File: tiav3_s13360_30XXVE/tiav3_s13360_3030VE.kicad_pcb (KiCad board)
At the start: 4 copper layers, 25.3 x 25.3 mm, 24 parts, among them J1 SSQ-103-01-G-D, J2 Conn_Coaxial, U1 OPA847IDBVT

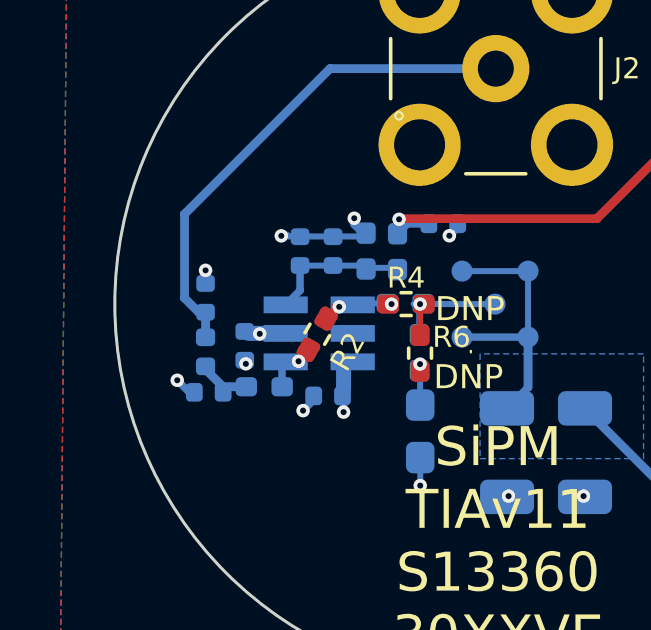
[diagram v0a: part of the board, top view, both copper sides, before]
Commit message: Switch all TIA boards to 0603 for the low pass inductor
0402 is fine for higher cutoffs but its hard to find >1000nH in 0402 without having high resistance.
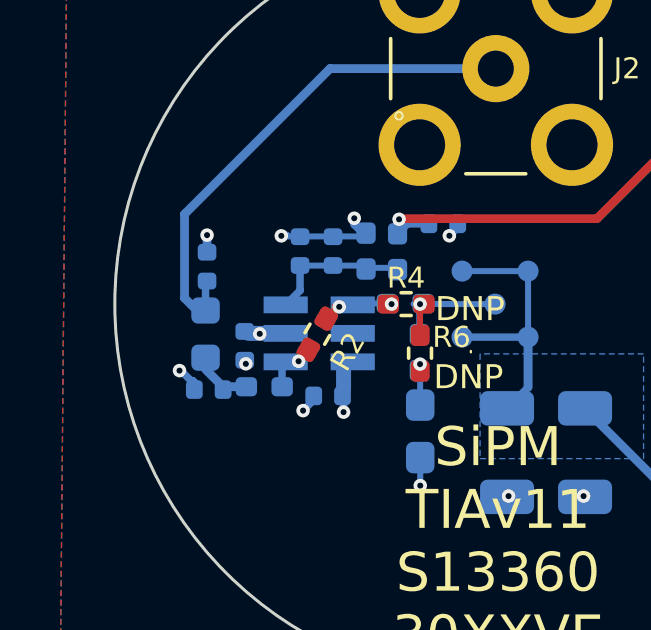
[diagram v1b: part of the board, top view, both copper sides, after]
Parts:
- D2: value s13360_3030VE -> s13360_3050VE
- L2: footprint Inductor_SMD:L_0402_1005Metric -> Inductor_SMD:L_0603_1608Metric
- moved C3 1.04 mm to (190.4, 98.8)
- moved L2 0.59 mm to (190.3, 101.0)
- moved C2 0.09 mm to (190.5, 102.8)
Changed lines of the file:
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@@
 		(tags "capacitor")
 		(property "Reference" "C7"
-			(at -0.167478 -1.2 90)
+			(at -0.067478 -1.15 90)
 			(layer "B.SilkS")
 			(effects
@@
 		(tags "capacitor")
 		(property "Reference" "C9"
-			(at -1.278 -0.036 0)
+			(at -1.590722 0.106 90)
 			(layer "B.SilkS")
 			(effects
@@
 	(footprint "Capacitor_SMD:C_0402_1005Metric"
 		(layer "B.Cu")
-		(at 190.35 99.790722 90)
+		(at 190.4 98.75 90)
 		(descr "Capacitor SMD 0402 (1005 Metric), square (rectangular) end terminal, IPC_7351 nominal, (Body size source: IPC-SM-782 page 76, https://www.pcb-3d.com/wordpress/wp-content/uploads/ipc-sm-782a_amendment_1_and_2.pdf), generated with kicad-footprint-generator")
 		(tags "capacitor")
@@
 			)
 		)
-		(property "Value" "s13360_3030VE"
+		(property "Value" "s13360_3050VE"
 			(at 0 2.45 0)
 			(unlocked yes)
@@
 	(footprint "Capacitor_SMD:C_0402_1005Metric"
 		(layer "B.Cu")
-		(at 190.456 102.940722 180)
+		(at 190.456 102.85 180)
 		(descr "Capacitor SMD 0402 (1005 Metric), square (rectangular) end terminal, IPC_7351 nominal, (Body size source: IPC-SM-782 page 76, https://www.pcb-3d.com/wordpress/wp-content/uploads/ipc-sm-782a_amendment_1_and_2.pdf), generated with kicad-footprint-generator")
 		(tags "capacitor")
@@
 		)
 	)
-	(footprint "Inductor_SMD:L_0402_1005Metric"
+	(footprint "Inductor_SMD:L_0603_1608Metric"
 		(layer "B.Cu")
-		(at 190.35 101.590722 90)
-		(descr "Inductor SMD 0402 (1005 Metric), square (rectangular) end terminal, IPC_7351 nominal, (Body size source: http://www.tortai-tech.com/upload/download/2011102023233369053.pdf), generated with kicad-footprint-generator")
+		(at 190.35 101 90)
+		(descr "Inductor SMD 0603 (1608 Metric), square (rectangular) end terminal, IPC-7351 nominal, (Body size source: http://www.tortai-tech.com/upload/download/2011102023233369053.pdf), generated with kicad-footprint-generator")
 		(tags "inductor")
 		(property "Reference" "L2"
-			(at 0.208 -0.846 90)
+			(at 0.025 -1.625 0)
 			(layer "B.SilkS")
 			(effects
 				(font
-					(size 0.7 0.7)
+					(size 1 1)
 					(thickness 0.15)
 				)
@@
 		)
 		(property "Value" "1500nH"
-			(at 0 -1.17 90)
+			(at 0 -1.43 270)
 			(layer "B.Fab")
 			(effects
@@
 		)
 		(property "Datasheet" ""
-			(at 0 0 90)
-			(layer "F.Fab")
+			(at 0 0 270)
+			(layer "B.Fab")
 			(hide yes)
 			(effects
@@
 					(thickness 0.15)
 				)
+				(justify mirror)
 			)
 		)
 		(property "Description" ""
-			(at 0 0 90)
-			(layer "F.Fab")
-			(hide yes)
-			(effects
-				(font
-					(size 1.27 1.27)
-					(thickness 0.15)
-				)
-			)
-		)
-		(property "part" "MLF1005GR56JTD25"
-			(at 291.940722 -88.759278 0)
+			(at 0 0 270)
 			(layer "B.Fab")
 			(hide yes)
 			(effects
 				(font
-					(size 1 1)
+					(size 1.27 1.27)
 					(thickness 0.15)
 				)
@@
 		(attr smd)
 		(fp_line
-			(start 0.93 -0.47)
-			(end -0.93 -0.47)
+			(start -0.162779 -0.51)
+			(end 0.162779 -0.51)
+			(stroke
+				(width 0.12)
+				(type solid)
+			)
+			(layer "B.SilkS")
+		)
+		(fp_line
+			(start -0.162779 0.51)
+			(end 0.162779 0.51)
+			(stroke
+				(width 0.12)
+				(type solid)
+			)
+			(layer "B.SilkS")
+		)
+		(fp_line
+			(start 1.48 -0.73)
+			(end -1.48 -0.73)
 			(stroke
 				(width 0.05)
@@
 		)
 		(fp_line
-			(start -0.93 -0.47)
-			(end -0.93 0.47)
+			(start -1.48 -0.73)
+			(end -1.48 0.73)
 			(stroke
 				(width 0.05)
@@
 		)
 		(fp_line
-			(start 0.93 0.47)
-			(end 0.93 -0.47)
+			(start 1.48 0.73)
+			(end 1.48 -0.73)
 			(stroke
 				(width 0.05)
@@
 		)
 		(fp_line
-			(start -0.93 0.47)
-			(end 0.93 0.47)
+			(start -1.48 0.73)
+			(end 1.48 0.73)
 			(stroke
 				(width 0.05)
@@
 		)
 		(fp_line
-			(start 0.5 -0.25)
-			(end -0.5 -0.25)
+			(start 0.8 -0.4)
+			(end -0.8 -0.4)
 			(stroke
 				(width 0.1)
@@
 		)
 		(fp_line
-			(start -0.5 -0.25)
-			(end -0.5 0.25)
+			(start -0.8 -0.4)
+			(end -0.8 0.4)
 			(stroke
 				(width 0.1)
@@
 		)
 		(fp_line
-			(start 0.5 0.25)
-			(end 0.5 -0.25)
+			(start 0.8 0.4)
+			(end 0.8 -0.4)
 			(stroke
 				(width 0.1)
@@
 		)
 		(fp_line
-			(start -0.5 0.25)
-			(end 0.5 0.25)
+			(start -0.8 0.4)
+			(end 0.8 0.4)
 			(stroke
 				(width 0.1)
@@
 		)
 		(fp_text user "${REFERENCE}"
-			(at 0 0 90)
+			(at 0 0 270)
 			(layer "B.Fab")
 			(effects
 				(font
-					(size 0.7 0.7)
-					(thickness 0.15)
+					(size 0.4 0.4)
+					(thickness 0.06)
 				)
 				(justify mirror)
@@
 		)
 		(pad "1" smd roundrect
-			(at -0.485 0 90)
-			(size 0.59 0.64)
+			(at -0.7875 0 90)
+			(size 0.875 0.95)
 			(layers "B.Cu" "B.Mask" "B.Paste")
 			(roundrect_rratio 0.25)
@@
 		)
 		(pad "2" smd roundrect
-			(at 0.485 0 90)
-			(size 0.59 0.64)
+			(at 0.7875 0 90)
+			(size 0.875 0.95)
 			(layers "B.Cu" "B.Mask" "B.Paste")
 			(roundrect_rratio 0.25)
@@
 		)
 		(embedded_fonts no)
-		(model "${KICAD6_3DMODEL_DIR}/Inductor_SMD.3dshapes/L_0402_1005Metric.wrl"
+		(model "${KICAD9_3DMODEL_DIR}/Inductor_SMD.3dshapes/L_0603_1608Metric.step"
 			(offset
 				(xyz 0 0 0)
@@
 	)
 	(via
-		(at 189.406 102.5382)
+		(at 189.481415 102.216362)
 		(size 0.45)
 		(drill 0.2)
@@
 	)
 	(via
-		(at 190.35 98.875)
+		(at 190.4 97.7)
 		(size 0.45)
 		(drill 0.2)
@@
 	)
 	(segment
-		(start 190.35 98.875)
-		(end 190.35 99.310722)
-		(width 0.29337)
-		(layer "B.Cu")
-		(net 1)
-	)
-	(segment
 		(start 195.306 97.353522)
 		(end 195.306 97.1382)
@@
 	)
 	(segment
+		(start 189.862046 102.551)
+		(end 189.926 102.551)
+		(width 0.25)
+		(layer "B.Cu")
+		(net 1)
+	)
+	(segment
+		(start 189.926 102.551)
+		(end 189.976 102.601)
+		(width 0.25)
+		(layer "B.Cu")
+		(net 1)
+	)
+	(segment
+		(start 189.976 102.601)
+		(end 189.976 102.940722)
+		(width 0.25)
+		(layer "B.Cu")
+		(net 1)
+	)
+	(segment
 		(start 198.755 97.325)
 		(end 198.755 97.442969)
@@
 	)
 	(segment
-		(start 189.976 102.940722)
-		(end 189.808522 102.940722)
+		(start 189.549 102.216362)
+		(end 189.549 102.237954)
 		(width 0.25)
 		(layer "B.Cu")
@@
 	)
 	(segment
-		(start 189.808522 102.940722)
-		(end 189.406 102.5382)
+		(start 189.481415 102.216362)
+		(end 189.549 102.216362)
+		(width 0.25)
+		(layer "B.Cu")
+		(net 1)
+	)
+	(segment
+		(start 190.4 97.7)
+		(end 190.4 98.27)
+		(width 0.29337)
+		(layer "B.Cu")
+		(net 1)
+	)
+	(segment
+		(start 189.549 102.237954)
+		(end 189.862046 102.551)
 		(width 0.25)
 		(layer "B.Cu")
@@
 	)
 	(segment
-		(start 189.65 97)
-		(end 189.65 99.8)
-		(width 0.29337)
+		(start 190.35 100.2125)
+		(end 190.35 99.28)
+		(width 0.25)
 		(layer "B.Cu")
 		(net 8)
 	)
 	(segment
-		(start 190.35 101.105722)
-		(end 190.35 100.270722)
+		(start 190.35 99.28)
+		(end 190.4 99.23)
+		(width 0.25)
+		(layer "B.Cu")
+		(net 8)
+	)
+	(segment
+		(start 189.65 97)
+		(end 189.65 99.8)
 		(width 0.29337)
 		(layer "B.Cu")
@@
 		(polygon
 			(pts
-				(xy 189.821 103.302522) (xy 192.276 103.302522) (xy 192.276 101.304322) (xy 190.975 101.3) (xy 191.0012 98.8)
-				(xy 189.825 98.8)
+				(xy 189.871 102.127522) (xy 192.326 102.127522) (xy 192.326 100.129322) (xy 191.025 100.125) (xy 191.0512 97.625)
+				(xy 189.875 97.625)
 			)
 		)
